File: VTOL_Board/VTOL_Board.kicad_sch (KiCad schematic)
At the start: 23 parts, among them J101 ICSP, J102 Servo1, SW101 RESET, SW102 START_SW, SW103 STOP/MODE_SW, U101 ATmega328P, Y101 16mHz

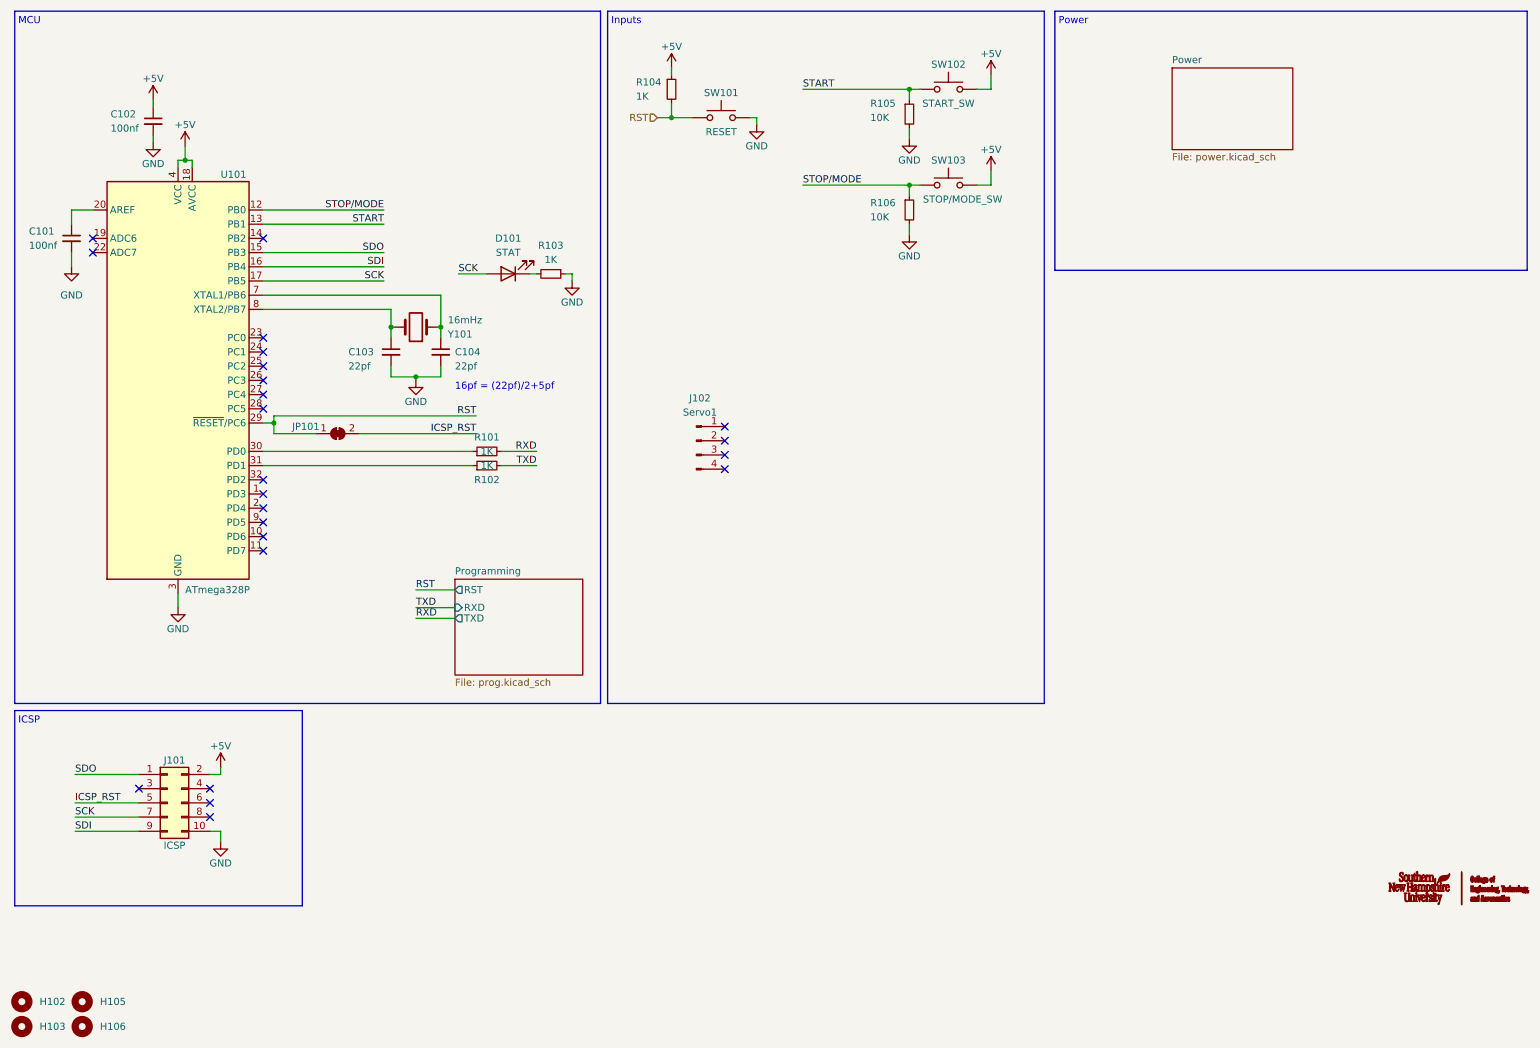
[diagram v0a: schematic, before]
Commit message: Change MCU
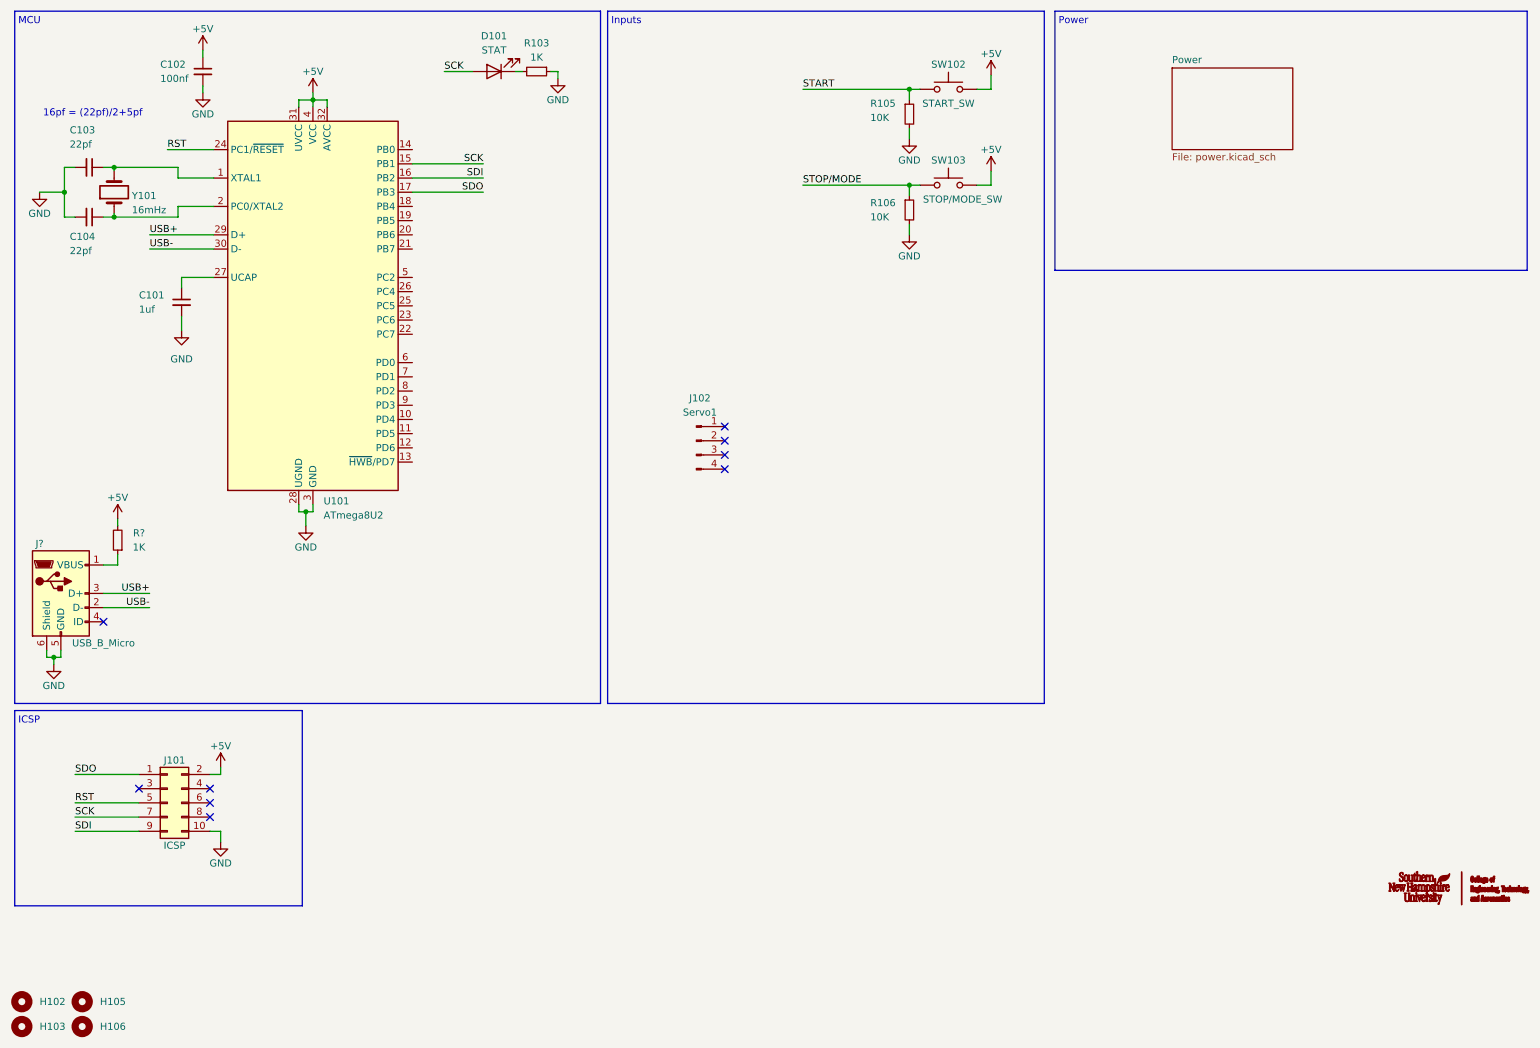
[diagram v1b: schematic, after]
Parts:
- removed JP101: RSTBridge, Jumper:SolderJumper-2_P1.3mm_Bridged_Pad1.0x1.5mm, symbol Jumper:SolderJumper_2_Bridged
- removed R101, R102, R104: 1K, Resistor_SMD:R_0805_2012Metric, symbol Device:R_Small
- removed SW101: RESET, Button_Switch_THT:SW_PUSH_6mm_H5mm, symbol Switch:SW_Push
- removed U101: ATmega328P, Package_QFP:TQFP-32_7x7mm_P0.8mm, symbol MCU_Microchip_ATmega:ATmega328P-A
- added J?: USB_B_Micro, Connector_USB:USB_Mini-B_Lumberg_2486_01_Horizontal, symbol Connector:USB_B_Micro
- added R?: 1K, Resistor_SMD:R_0805_2012Metric, symbol Device:R_Small
- added U101: ATmega8U2, Package_QFP:TQFP-32_7x7mm_P0.8mm, symbol MCU_Microchip_ATmega:ATmega8U2-A
- C101: value 100nf -> 1uf
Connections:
- net ICSP_RST is gone; now on net RST: J101.5 (Pin_5)
- net +5V: now also R?.2, U101.31 (UVCC), U101.32 (AVCC), U101.4 (VCC)
- net GND: now also J?.5 (GND), J?.6 (Shield), U101.28 (UGND), U101.3 (GND)
- net RST: now also U101.24 (PC1/~{RESET})
- net SCK: now also U101.15 (PB1)
- net SDI: now also U101.16 (PB2)
- net SDO: now also U101.17 (PB3)
- net at C101.1: now also U101.27 (UCAP)
- net at C103.1, Y101.2: now also U101.1 (XTAL1)
- net at C104.1, Y101.1: now also U101.2 (PC0/XTAL2)
- new net: J?.1 (VBUS), R?.1
- new net USB+: J?.3 (D+), U101.29 (D+)
- new net USB-: J?.2 (D-), U101.30 (D-)
- no-connect marks 23 -> 9
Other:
- removed sheet Programming
- moved on the sheet: C102, D101, R103
